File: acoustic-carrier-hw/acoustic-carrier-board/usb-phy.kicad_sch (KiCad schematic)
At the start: 52 parts, among them J801 TYPE-C-31-M-12, U801 USB3300-EZK, U802 LMV321, Y801 Crystal_GND24_Small

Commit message: [carrier] Routing out RGMII interface
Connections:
- net USB_DM renamed USB_D-
- net USB_DP renamed USB_D+
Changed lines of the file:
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@@
 		)
 	)
-	(label "USB_DP"
+	(label "USB_D+"
 		(at 181.61 74.93 0)
 		(effects
@@
 		)
 	)
-	(label "USB_DM"
+	(label "USB_D-"
 		(at 181.61 77.47 0)
 		(effects

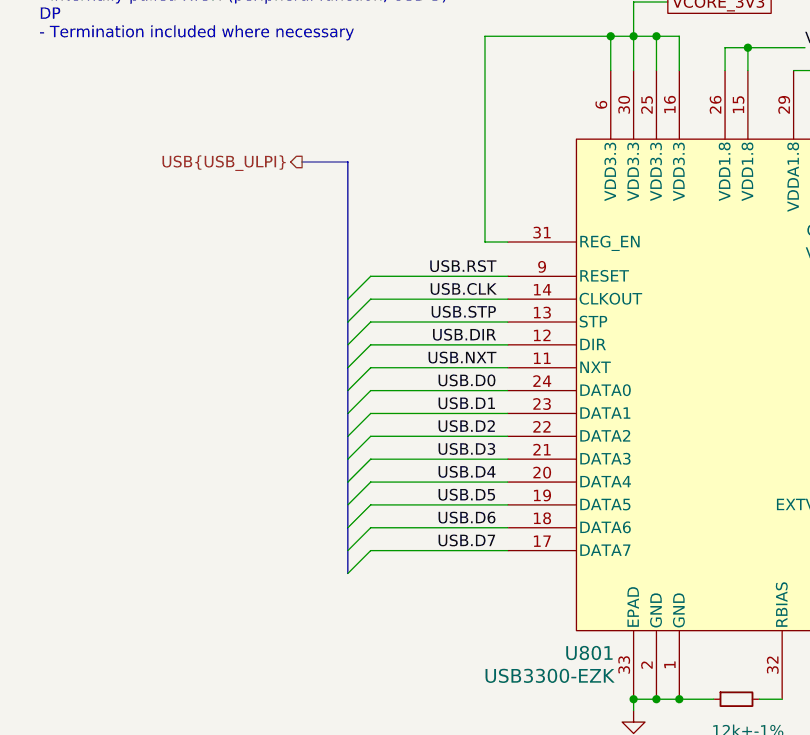
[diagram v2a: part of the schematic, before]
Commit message: [carrier] Changed all vias to (pcheaper) 0.2/0.35 size (next) create basic test-VHDL for clock-signal fanout checks
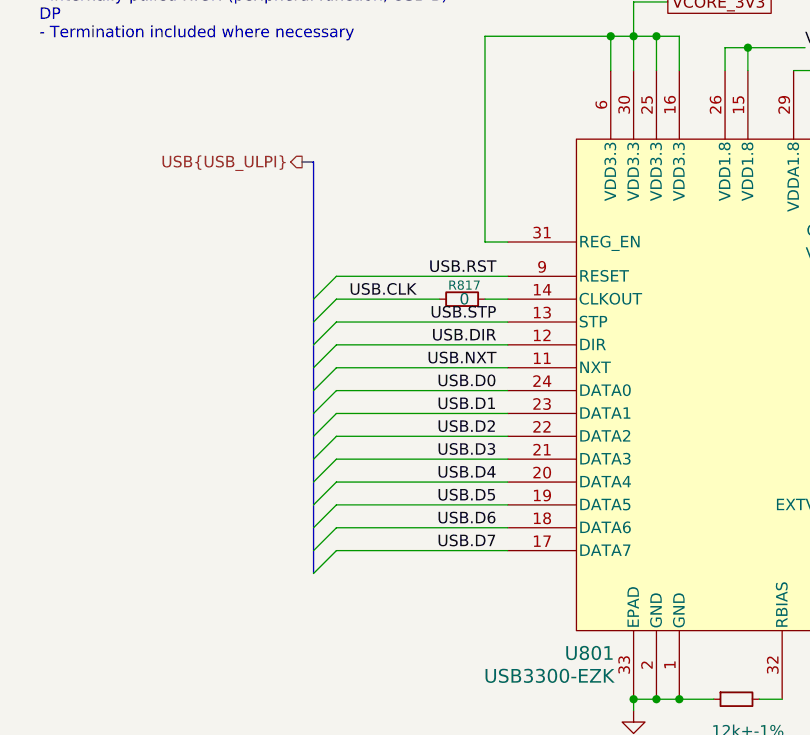
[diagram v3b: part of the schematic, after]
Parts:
- added R817: 0, Resistor_SMD:R_0603_1608Metric, symbol Device:R_Small
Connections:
- net USB.CLK: now also R817.2; no longer U801.14 (CLKOUT)
- new net: R817.1, U801.14 (CLKOUT)

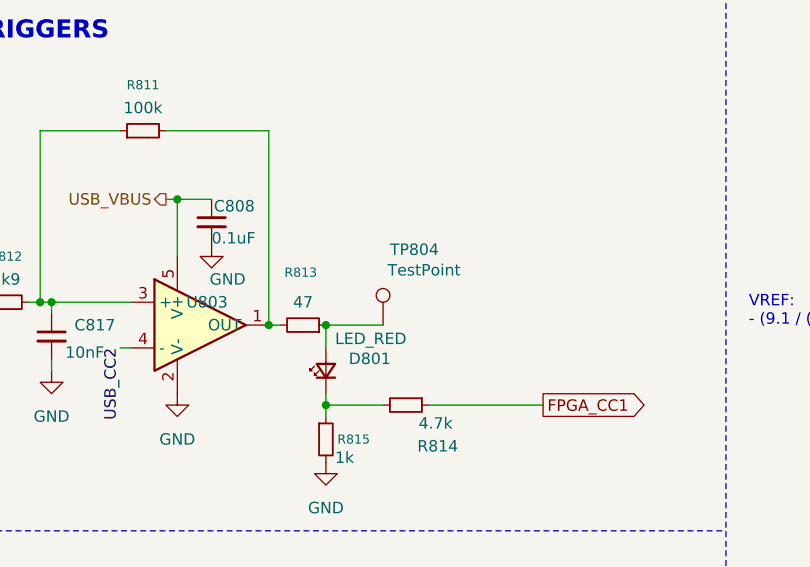
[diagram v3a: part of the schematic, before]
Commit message: [carrier] Added extra decoupling to ADC bias voltage
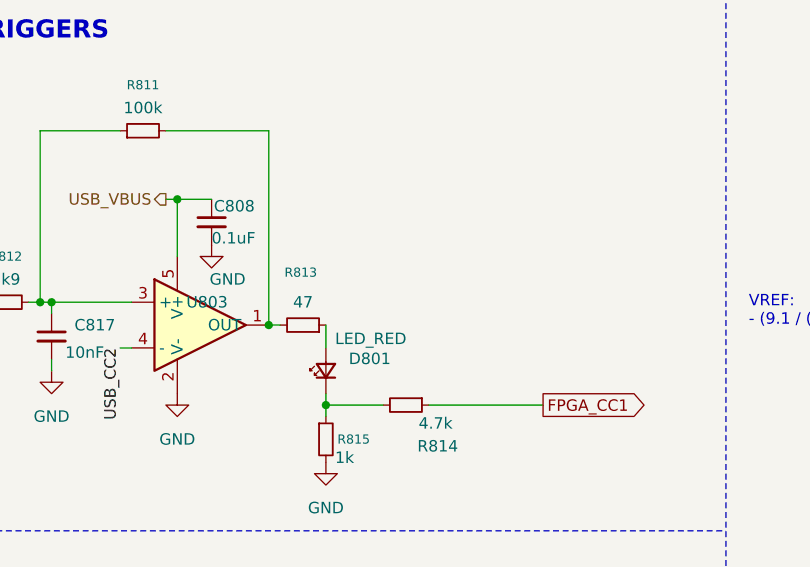
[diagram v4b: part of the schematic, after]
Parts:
- removed TP804: TestPoint, TestPoint:TestPoint_Loop_D1.80mm_Drill1.0mm_Beaded, symbol Connector:TestPoint
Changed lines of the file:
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@@
 	)
 	(junction
-		(at 285.75 172.72)
-		(diameter 0)
-		(color 0 0 0 0)
-	)
-	(junction
 		(at 102.87 177.8)
 		(diameter 0)
@@
 	(wire
 		(pts
-			(xy 285.75 172.72) (xy 292.1 172.72)
-		)
-		(stroke
-			(width 0)
-			(type default)
-		)
-	)
-	(wire
-		(pts
 			(xy 165.1 41.91) (xy 185.42 41.91)
 		)
@@
 					(unit 1)
 				)
-			)
-		)
-	)
-	(symbol
-		(lib_id "Connector:TestPoint")
-		(at 292.1 172.72 0)
-		(unit 1)
-		(exclude_from_sim no)
-		(in_bom yes)
-		(on_board yes)
-		(dnp no)
-		(property "Reference" "TP804"
-			(at 292.862 164.338 0)
-			(effects
-				(font
-					(size 1.27 1.27)
-				)
-				(justify left)
-			)
-		)
-		(property "Value" "TestPoint"
-			(at 292.608 166.624 0)
-			(effects
-				(font
-					(size 1.27 1.27)
-				)
-				(justify left)
-			)
-		)
-		(property "Footprint" "TestPoint:TestPoint_Loop_D1.80mm_Drill1.0mm_Beaded"
-			(at 297.18 172.72 0)
-			(effects
-				(font
-					(size 1.27 1.27)
-				)
-				(hide yes)
-			)
-		)
-		(property "Datasheet" "~"
-			(at 297.18 172.72 0)
-			(effects
-				(font
-					(size 1.27 1.27)
-				)
-				(hide yes)
-			)
-		)
-		(property "Description" "test point"
-			(at 292.1 172.72 0)
-			(effects
-				(font
-					(size 1.27 1.27)
-				)
-				(hide yes)
-			)
-		)
-		(pin "1"
-		)
-		(instances
-			(project "acoustic-carrier-board"
-				(path "/25b015c9-ab13-4427-b72c-b6f348597100/bccc7554-d2b1-4102-8d28-ddff56ec5c7a"
-					(reference "TP804")
-					(unit 1)
-				)
